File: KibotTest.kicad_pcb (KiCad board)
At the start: 2 copper layers, 16 x 10.8 mm, 3 parts, among them J1 Conn_01x02

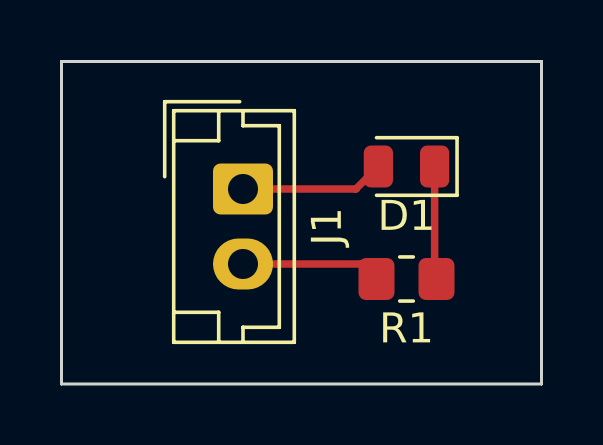
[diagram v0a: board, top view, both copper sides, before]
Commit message: [ROOT] Implement Github Actions + Fix README.md
[FIX] Update README images

[NEW] Add schematics

[ACT] Try to use github actions

[ACT] Move to the good folder

[ACT] First test of action

[GEN] Remove generated for test

[ACT] Fix variant

[ACT] 2nd test

[ACT] 3rd test

[ACT] 3rd test (really this one)

[ACT] 4th test

[ACT] 4th test (really again....)

[ACT] 5th test

[ACT] 6th test

[ACT] 7th test

[ACT] 7th test (really)

[ACT] 8th test (maybe)

[ACT] test

[ACT] Fix run

[CI] Auto-release exports files

[ACT] Fix ERC

[ACT] Fix add -f

[CI] Auto-release exports files

[PCB] Edit PCB

[CI] Auto-release exports files
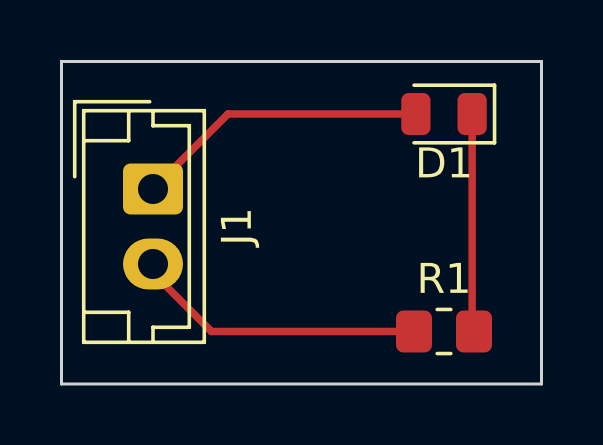
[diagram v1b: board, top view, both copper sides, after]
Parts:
- moved J1 3.00 mm to (48.8, 48.2)
- moved D1 2.15 mm to (58.5, 45.8)
- moved R1 2.15 mm to (58.5, 53.0)
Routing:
- net GND: track 4.66 -> 9.81 mm
- net +5V: track 4.82 -> 9.80 mm
- net Net-(D1-Pad1): track 3.78 -> 7.28 mm
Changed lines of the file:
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@@
   (net 3 "GND")
   (footprint "LED_SMD:LED_0805_2012Metric" (layer "F.Cu")
-    (at 57.25 47.5 180)
+    (at 58.5 45.75 180)
     (descr "LED SMD 0805 (2012 Metric), square (rectangular) end terminal, IPC_7351 nominal, (Body size source: https://docs.google.com/spreadsheets/d/1BsfQQcO9C6DZCsRaXUlFlo91Tg2WpOkGARC1WS5S8t0/edit?usp=sharing), generated with kicad-footprint-generator")
     (tags "LED")
@@
   )
   (footprint "Connector_JST:JST_EH_B2B-EH-A_1x02_P2.50mm_Vertical" (layer "F.Cu")
-    (at 51.8 48.25 -90)
+    (at 48.8 48.25 -90)
     (descr "JST EH series connector, B2B-EH-A (http://www.jst-mfg.com/product/pdf/eng/eEH.pdf), generated with kicad-footprint-generator")
     (tags "connector JST EH vertical")
@@
   )
   (footprint "Resistor_SMD:R_0805_2012Metric_Pad1.20x1.40mm_HandSolder" (layer "F.Cu")
-    (at 57.25 51.25 180)
+    (at 58.5 53 180)
     (descr "Resistor SMD 0805 (2012 Metric), square (rectangular) end terminal, IPC_7351 nominal with elongated pad for handsoldering. (Body size source: IPC-SM-782 page 72, https://www.pcb-3d.com/wordpress/wp-content/uploads/ipc-sm-782a_amendment_1_and_2.pdf), generated with kicad-footprint-generator")
     (tags "resistor handsolder")
@@
     (property "Sheetname" "")
     (attr smd)
-    (fp_text reference "R1" (at 0 -1.65) (layer "F.SilkS")
+    (fp_text reference "R1" (at 0 1.75) (layer "F.SilkS")
       (effects (font (size 1 1) (thickness 0.15)))
     )
-    (fp_text value "R" (at 0 1.65) (layer "F.Fab")
+    (fp_text value "R" (at 2.25 0) (layer "F.Fab")
       (effects (font (size 1 1) (thickness 0.15)))
     )
@@
   )
   (gr_rect (start 61.75 54.75) (end 45.75 44) (layer "Edge.Cuts") (width 0.1) (fill none))
-  (segment (start 58.1875 47.5) (end 58.1875 51.1875) (width 0.25) (layer "F.Cu") (net 1))
-  (segment (start 58.1875 51.1875) (end 58.25 51.25) (width 0.25) (layer "F.Cu") (net 1))
-  (segment (start 55.5625 48.25) (end 56.3125 47.5) (width 0.25) (layer "F.Cu") (net 2))
-  (segment (start 51.8 48.25) (end 55.5625 48.25) (width 0.25) (layer "F.Cu") (net 2))
-  (segment (start 56.25 51.25) (end 55.75 50.75) (width 0.25) (layer "F.Cu") (net 3))
-  (segment (start 55.75 50.75) (end 51.8 50.75) (width 0.25) (layer "F.Cu") (net 3))
+  (segment (start 59.4375 52.9375) (end 59.5 53) (width 0.25) (layer "F.Cu") (net 1))
+  (segment (start 59.4375 45.75) (end 59.4375 52.9375) (width 0.25) (layer "F.Cu") (net 1))
+  (segment (start 51.3 45.75) (end 48.8 48.25) (width 0.25) (layer "F.Cu") (net 2))
+  (segment (start 57.5625 45.75) (end 51.3 45.75) (width 0.25) (layer "F.Cu") (net 2))
+  (segment (start 57.5 53) (end 50.75 53) (width 0.25) (layer "F.Cu") (net 3))
+  (segment (start 48.8 51.05) (end 48.8 50.75) (width 0.25) (layer "F.Cu") (net 3))
+  (segment (start 50.75 53) (end 48.8 51.05) (width 0.25) (layer "F.Cu") (net 3))
   (zone (net 3) (net_name "GND") (layers F&B.Cu) (hatch edge 0.508)
     (connect_pads (clearance 0.508))

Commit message: [ACT] Test error detection
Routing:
- net +5V: track 9.80 -> 0.00 mm
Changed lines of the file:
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@@
   (segment (start 59.4375 52.9375) (end 59.5 53) (width 0.25) (layer "F.Cu") (net 1))
   (segment (start 59.4375 45.75) (end 59.4375 52.9375) (width 0.25) (layer "F.Cu") (net 1))
-  (segment (start 51.3 45.75) (end 48.8 48.25) (width 0.25) (layer "F.Cu") (net 2))
-  (segment (start 57.5625 45.75) (end 51.3 45.75) (width 0.25) (layer "F.Cu") (net 2))
   (segment (start 57.5 53) (end 50.75 53) (width 0.25) (layer "F.Cu") (net 3))
   (segment (start 48.8 51.05) (end 48.8 50.75) (width 0.25) (layer "F.Cu") (net 3))

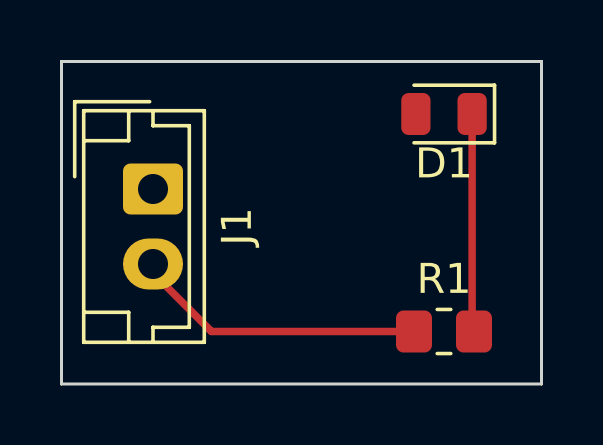
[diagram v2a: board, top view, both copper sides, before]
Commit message: Revert "[ACT] Test error detection"
This reverts commit 250b70cec5ef92d058678cda262f443f8b6e7f6b.
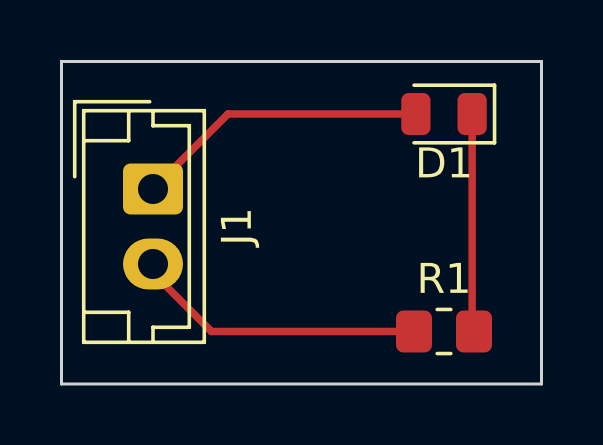
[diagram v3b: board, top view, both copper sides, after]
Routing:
- net +5V: track 0.00 -> 9.80 mm
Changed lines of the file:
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@@
   (segment (start 59.4375 52.9375) (end 59.5 53) (width 0.25) (layer "F.Cu") (net 1))
   (segment (start 59.4375 45.75) (end 59.4375 52.9375) (width 0.25) (layer "F.Cu") (net 1))
+  (segment (start 51.3 45.75) (end 48.8 48.25) (width 0.25) (layer "F.Cu") (net 2))
+  (segment (start 57.5625 45.75) (end 51.3 45.75) (width 0.25) (layer "F.Cu") (net 2))
   (segment (start 57.5 53) (end 50.75 53) (width 0.25) (layer "F.Cu") (net 3))
   (segment (start 48.8 51.05) (end 48.8 50.75) (width 0.25) (layer "F.Cu") (net 3))
